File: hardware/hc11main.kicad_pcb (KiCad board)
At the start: 2 copper layers, 100 x 71 mm, 31 parts, among them P1 CONN_2X20, U10 74LS10, U11 27256, U12 74LS245, U13 74LS245, U2 68HC11A0_PLCC, U3 74LS573, U4 74LS138, U5 74LS245, U6 74LS00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

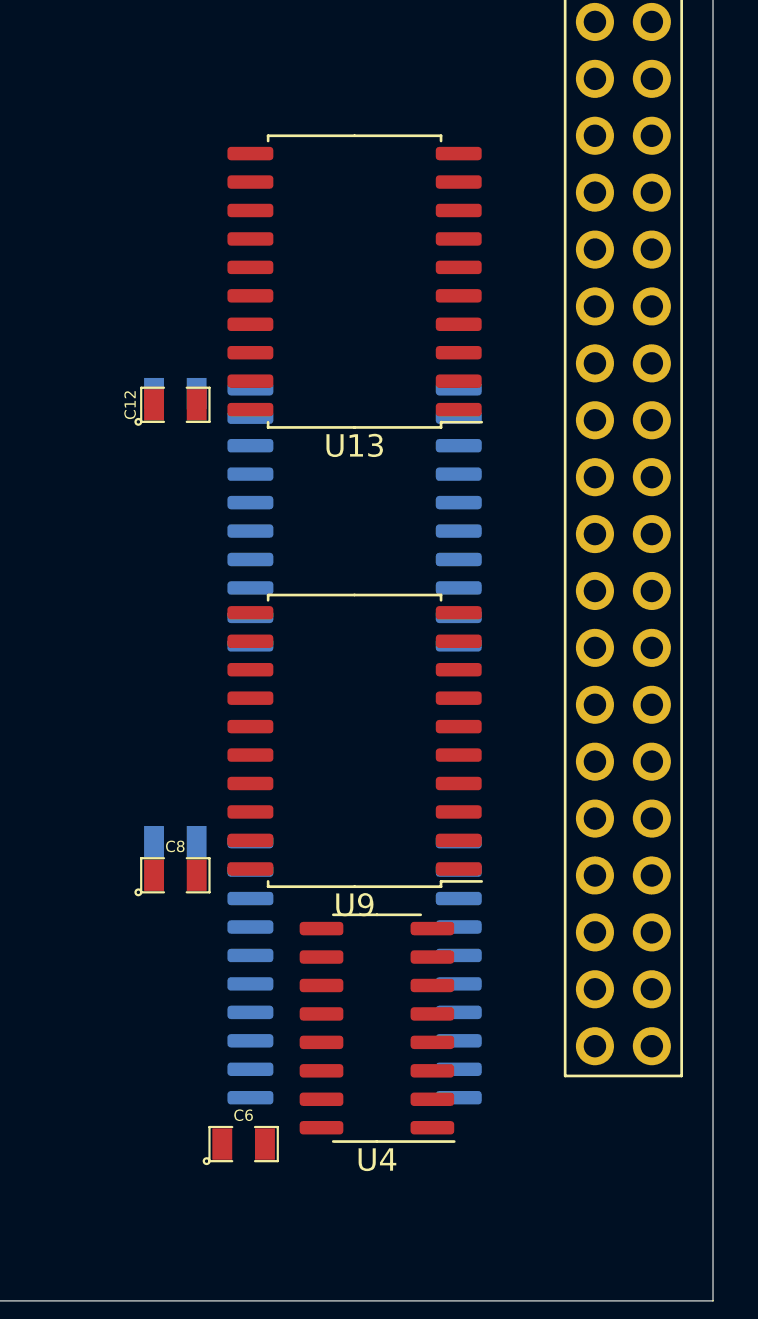
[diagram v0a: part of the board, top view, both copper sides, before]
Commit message: same address scheme in C, compute asm flags, we're close
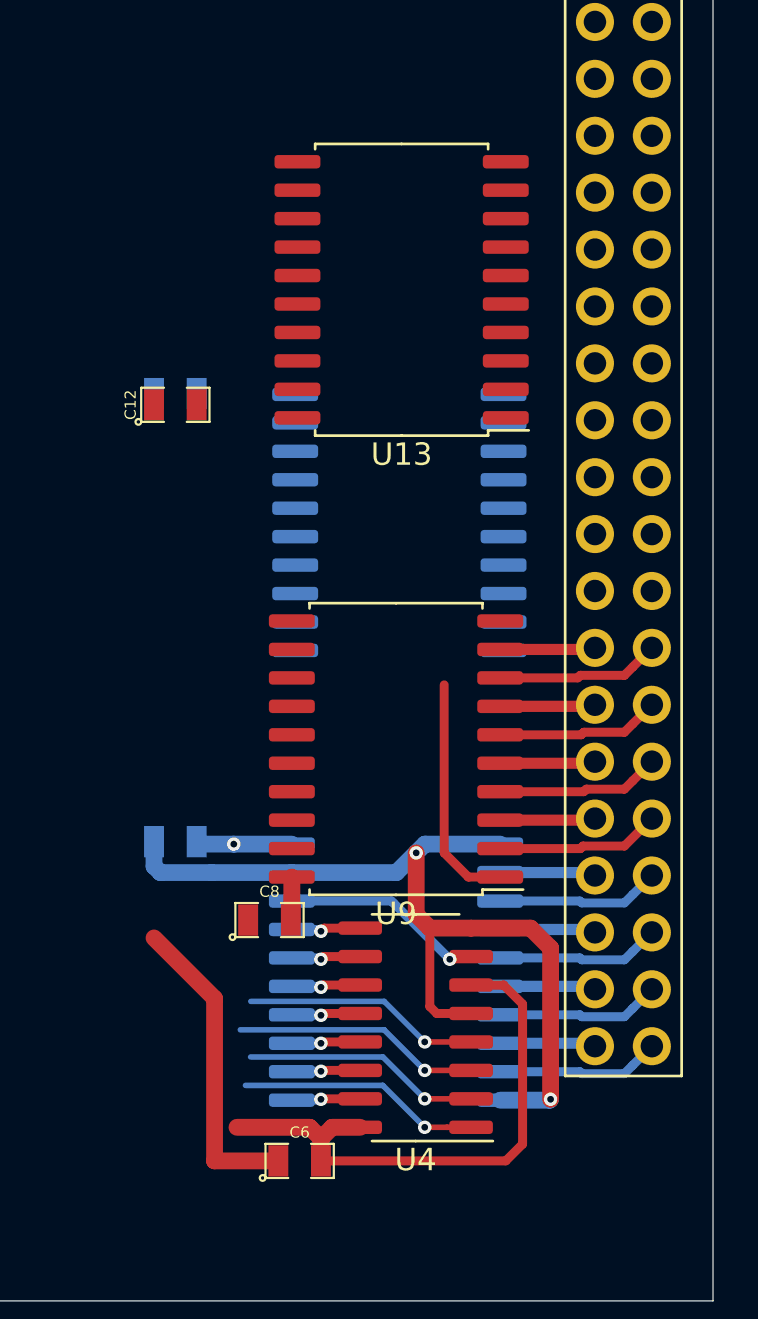
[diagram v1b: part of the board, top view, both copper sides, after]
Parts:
- moved C8 4.65 mm to (95.2, 69.0)
- moved C6 2.61 mm to (96.5, 79.8)
- moved U13 2.13 mm to (101.1, 40.9)
- moved U12 2.02 mm to (101.0, 51.2)
- moved U9 1.89 mm to (100.8, 61.4)
- moved U5 1.85 mm to (100.8, 71.3)
- moved U4 1.73 mm to (101.7, 73.8)
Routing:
- net GND: track 0.00 -> 55.0 mm, vias 0 -> 2
- net VCC: track 0.00 -> 31.4 mm, vias 0 -> 1
- net /A12: track 0.00 -> 11.0 mm, vias 0 -> 1
- net /A10: track 0.00 -> 10.8 mm, vias 0 -> 1
- net /A11: track 0.00 -> 10.6 mm, vias 0 -> 1
- net /~CSIO: track 0.00 -> 10.6 mm, vias 0 -> 1
- net /R~W: track 0.00 -> 10.4 mm
- net /S7: track 0.00 -> 9.13 mm, vias 0 -> 1
- net /bD2: track 0.00 -> 7.33 mm
- net /bD0: track 0.00 -> 7.33 mm
- net /bD6: track 0.00 -> 7.33 mm
- net /bD4: track 0.00 -> 7.33 mm
- net /bS4: track 0.00 -> 7.31 mm
- net /bS0: track 0.00 -> 7.31 mm
- net /bS6: track 0.00 -> 7.31 mm
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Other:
- net class Default: clearance 0.2 -> 0.175; via_dia 0.8 -> 0.6; via_drill 0.4 -> 0.3
- rule trace_clearance: 0.2 -> 0.175
- rule via_min_size: 0.4 -> 0.6
